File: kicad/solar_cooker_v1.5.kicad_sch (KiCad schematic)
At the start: 28 parts, among them J1 Pt100, J10 SSQ-108-01-G-S, J11 SSQ-108-01-G-S, J12 SSQ-108-01-G-S, J13 SSQ-118-01-G-D, J14 SSQ-108-01-G-S, J15 SSQ-108-01-G-S, J16 SSQ-110-01-G-S, J4 Pt100, J6 GPS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

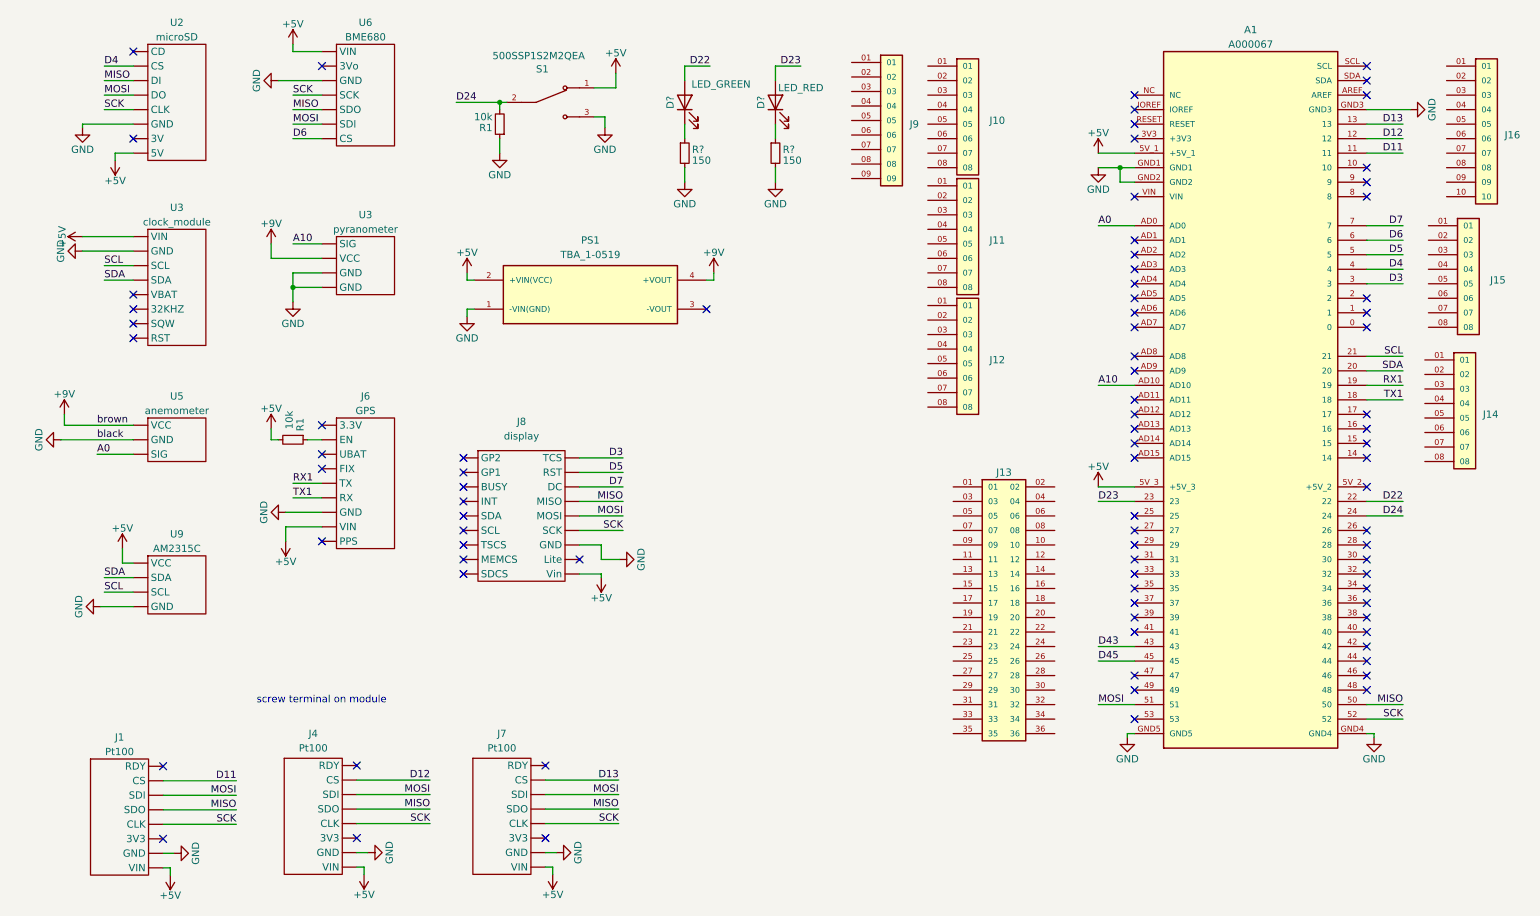
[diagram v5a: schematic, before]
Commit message: minor silkscreen fix
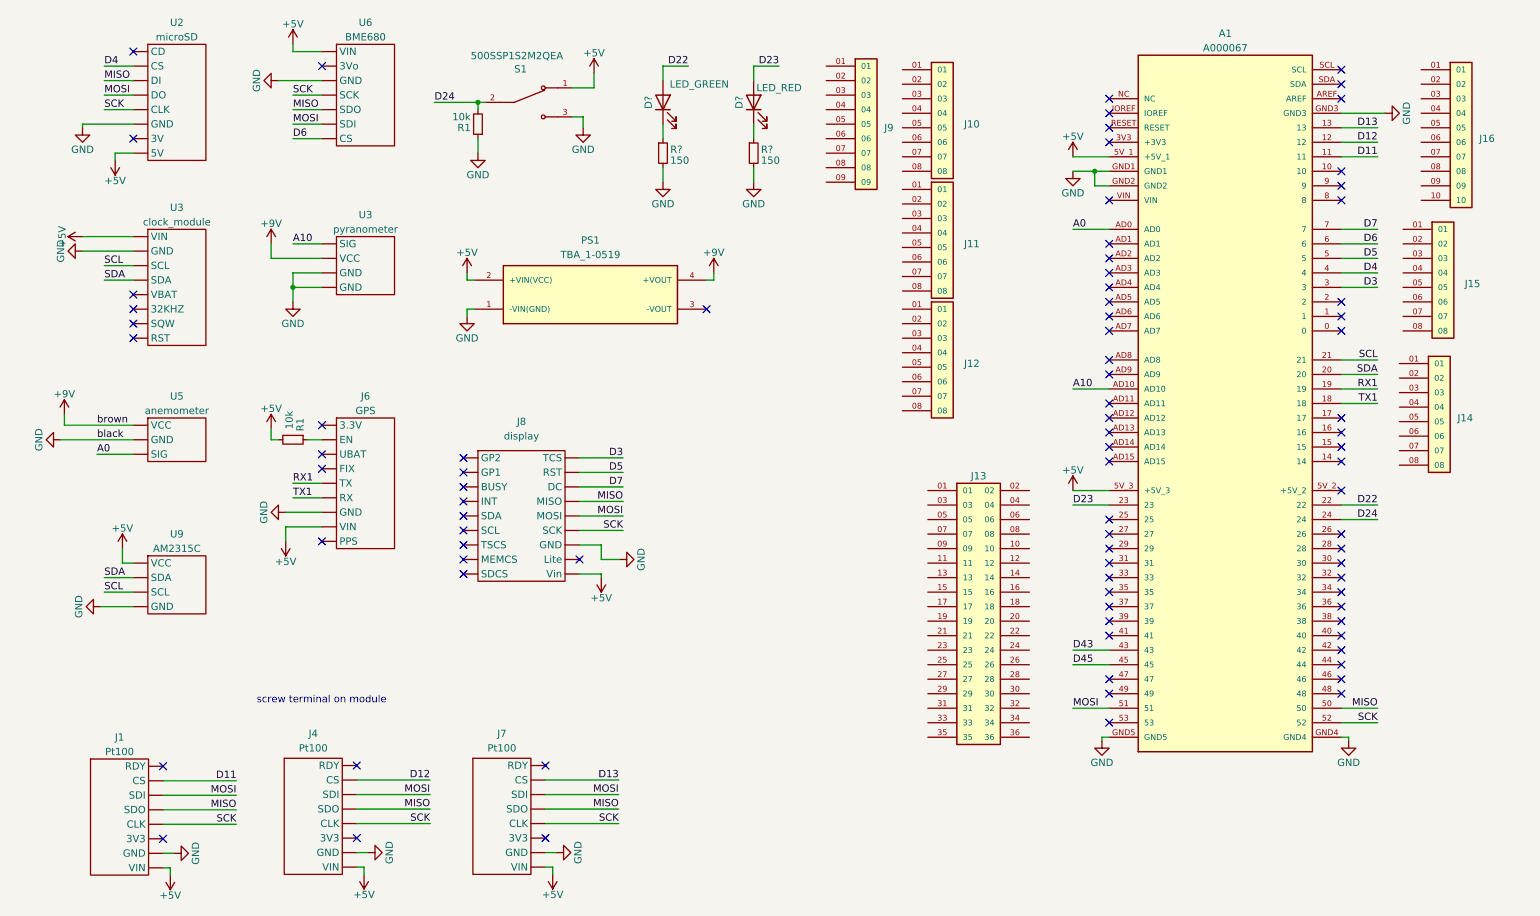
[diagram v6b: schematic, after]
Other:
- moved on the sheet: A1, D?, J10, J11, J12, J13, J14, J15, J16, J9, R1, R?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

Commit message: order v2
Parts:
- D? (x2): footprint (none) -> LED_SMD:LED_1206_3216Metric_Pad1.42x1.75mm_HandSolder
- J1, J4, J7: footprint custom_components:Pt100 -> custom_components:PT100
- J6: footprint (none) -> custom_components:GPS
- J8: footprint (none) -> custom_components:display
- PS1: footprint CONV_TBA_1-0519 -> TBA_1-0519:CONV_TBA_1-0519; MANUFACTURER Traco Power -> (none); MAXIMUM_PACKAGE_HEIGHT 10.15mm -> (none); PARTREV April 19, 2021 -> (none); STANDARD Manufacturer Recommendations -> (none)
- R1, R? (x2): footprint (none) -> Resistor_SMD:R_1206_3216Metric_Pad1.30x1.75mm_HandSolder
- U2: footprint (none) -> custom_components:microSD
- U3, U9: footprint (none) -> custom_components:screw_terminal_4pin
- U3: footprint (none) -> custom_components:clock_module
- U5: footprint (none) -> custom_components:screw_terminal_3pin
- U6: footprint (none) -> custom_components:BME680
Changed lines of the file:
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@@
     (stroke (width 0) (type default) (color 255 0 0 1))
+  )
+  (wire (pts (xy 208.915 57.785) (xy 215.265 57.785))
+    (stroke (width 0) (type default))
   )
   (wire (pts (xy 153.035 46.99) (xy 153.035 49.53))
@@
     (stroke (width 0) (type default))
   )
-  (wire (pts (xy 208.915 57.785) (xy 215.265 57.785))
-    (stroke (width 0) (type default))
-  )
   (wire (pts (xy 38.735 123.825) (xy 44.45 123.825))
     (stroke (width 0) (type default) (color 1 1 1 1))
@@
     (effects (font (size 1.27 1.27)) (justify left bottom))
   )
+  (label "A0" (at 208.915 57.785 0) (fields_autoplaced)
+    (effects (font (size 1.27 1.27)) (justify left bottom))
+  )
   (label "SCK" (at 62.484 161.925 180) (fields_autoplaced)
     (effects (font (size 1.27 1.27)) (justify right bottom))
@@
     (effects (font (size 1.27 1.27)) (justify left bottom))
   )
-  (label "A0" (at 208.915 57.785 0) (fields_autoplaced)
-    (effects (font (size 1.27 1.27)) (justify left bottom))
-  )
   (label "D12" (at 96.393 154.178 180) (fields_autoplaced)
     (effects (font (size 1.27 1.27)) (justify right bottom))
@@
       (effects (font (size 1.27 1.27)))
     )
-    (property "Footprint" "" (at 112.395 93.98 0)
+    (property "Footprint" "custom_components:display" (at 112.395 93.98 0)
       (effects (font (size 1.27 1.27)) hide)
     )
@@
       (effects (font (size 1.27 1.27)))
     )
-    (property "Footprint" "" (at 49.53 117.475 0)
+    (property "Footprint" "custom_components:screw_terminal_4pin" (at 49.53 117.475 0)
       (effects (font (size 1.27 1.27)) hide)
     )
@@
       (effects (font (size 1.27 1.27)) (justify left))
     )
-    (property "Footprint" "" (at 104.775 39.37 0)
+    (property "Footprint" "Resistor_SMD:R_1206_3216Metric_Pad1.30x1.75mm_HandSolder" (at 104.775 39.37 0)
       (effects (font (size 1.27 1.27)) hide)
     )
@@
       (effects (font (size 1.27 1.27)))
     )
-    (property "Footprint" "" (at 153.035 35.56 0)
+    (property "Footprint" "LED_SMD:LED_1206_3216Metric_Pad1.42x1.75mm_HandSolder" (at 153.035 35.56 0)
       (effects (font (size 1.27 1.27)) hide)
     )
@@
       (effects (font (size 1.27 1.27)) (justify left))
     )
-    (property "Footprint" "" (at 72.39 94.615 0)
+    (property "Footprint" "Resistor_SMD:R_1206_3216Metric_Pad1.30x1.75mm_HandSolder" (at 72.39 94.615 0)
       (effects (font (size 1.27 1.27)) hide)
     )
@@
       (effects (font (size 1.27 1.27)))
     )
-    (property "Footprint" "" (at 52.07 27.94 0)
+    (property "Footprint" "custom_components:microSD" (at 52.07 27.94 0)
       (effects (font (size 1.27 1.27)) hide)
     )
@@
       (effects (font (size 1.27 1.27)) (justify left))
     )
-    (property "Footprint" "" (at 153.035 44.45 0)
+    (property "Footprint" "Resistor_SMD:R_1206_3216Metric_Pad1.30x1.75mm_HandSolder" (at 153.035 44.45 0)
       (effects (font (size 1.27 1.27)) hide)
     )
@@
       (effects (font (size 1.27 1.27)))
     )
-    (property "Footprint" "custom_components:Pt100" (at 73.406 149.098 0)
+    (property "Footprint" "custom_components:PT100" (at 73.406 149.098 0)
       (effects (font (size 1.27 1.27)) hide)
     )
@@
       (effects (font (size 1.27 1.27)))
     )
-    (property "Footprint" "" (at 137.16 35.56 0)
+    (property "Footprint" "LED_SMD:LED_1206_3216Metric_Pad1.42x1.75mm_HandSolder" (at 137.16 35.56 0)
       (effects (font (size 1.27 1.27)) hide)
     )
@@
       (effects (font (size 1.27 1.27)))
     )
-    (property "Footprint" "" (at 85.09 60.325 0)
+    (property "Footprint" "custom_components:screw_terminal_4pin" (at 85.09 60.325 0)
       (effects (font (size 1.27 1.27)) hide)
     )
@@
       (effects (font (size 1.27 1.27)))
     )
-    (property "Footprint" "custom_components:Pt100" (at 39.497 149.225 0)
+    (property "Footprint" "custom_components:PT100" (at 39.497 149.225 0)
       (effects (font (size 1.27 1.27)) hide)
     )
@@
       (effects (font (size 1.27 1.27)))
     )
-    (property "Footprint" "custom_components:Pt100" (at 106.426 149.098 0)
+    (property "Footprint" "custom_components:PT100" (at 106.426 149.098 0)
       (effects (font (size 1.27 1.27)) hide)
     )
@@
       (effects (font (size 1.27 1.27)) (justify left))
     )
-    (property "Footprint" "" (at 137.16 44.45 0)
+    (property "Footprint" "Resistor_SMD:R_1206_3216Metric_Pad1.30x1.75mm_HandSolder" (at 137.16 44.45 0)
       (effects (font (size 1.27 1.27)) hide)
     )
@@
       (effects (font (size 1.27 1.27)))
     )
-    (property "Footprint" "" (at 53.34 98.425 0)
+    (property "Footprint" "custom_components:screw_terminal_3pin" (at 53.34 98.425 0)
       (effects (font (size 1.27 1.27)) hide)
     )
@@
   (symbol (lib_id "A000067:A000067") (at 235.585 88.265 0) (unit 1)
     (in_bom no) (on_board yes) (dnp no) (fields_autoplaced)
-    (property "Reference" "A1" (at 235.585 23.495 0)
-      (effects (font (size 1.27 1.27)))
-    )
-    (property "Value" "A000067" (at 235.585 26.035 0)
+    (property "Reference" "A1" (at 235.585 22.86 0)
+      (effects (font (size 1.27 1.27)))
+    )
+    (property "Value" "A000067" (at 235.585 25.4 0)
       (effects (font (size 1.27 1.27)))
     )
@@
     (pin "8")
     (pin "9")
-    (pin "AD0")
     (pin "AD1")
     (pin "AD10")
@@
     (pin "SDA")
     (pin "VIN")
+    (pin "AD0")
     (instances
       (project "solar_cooker_v1.5"
@@
       (effects (font (size 1.27 1.27)))
     )
-    (property "Footprint" "" (at 87.63 34.29 0)
+    (property "Footprint" "custom_components:BME680" (at 87.63 34.29 0)
       (effects (font (size 1.27 1.27)) hide)
     )
@@
       (effects (font (size 1.27 1.27)))
     )
-    (property "Footprint" "" (at 85.09 90.805 0)
+    (property "Footprint" "custom_components:GPS" (at 85.09 90.805 0)
       (effects (font (size 1.27 1.27)) hide)
     )
@@
       (effects (font (size 1.27 1.27)))
     )
-    (property "Footprint" "" (at 52.07 67.945 0)
+    (property "Footprint" "custom_components:clock_module" (at 52.07 67.945 0)
       (effects (font (size 1.27 1.27)) hide)
     )
@@
       (effects (font (size 1.27 1.27)))
     )
-    (property "Footprint" "CONV_TBA_1-0519" (at 124.46 69.215 0)
+    (property "Footprint" "TBA_1-0519:CONV_TBA_1-0519" (at 124.46 69.215 0)
       (effects (font (size 1.27 1.27)) (justify bottom) hide)
     )
@@
       (effects (font (size 1.27 1.27)) hide)
     )
-    (property "PARTREV" "April 19, 2021" (at 124.46 69.215 0)
-      (effects (font (size 1.27 1.27)) (justify bottom) hide)
-    )
-    (property "STANDARD" "Manufacturer Recommendations" (at 124.46 69.215 0)
-      (effects (font (size 1.27 1.27)) (justify bottom) hide)
-    )
-    (property "MAXIMUM_PACKAGE_HEIGHT" "10.15mm" (at 124.46 69.215 0)
-      (effects (font (size 1.27 1.27)) (justify bottom) hide)
-    )
-    (property "MANUFACTURER" "Traco Power" (at 124.46 69.215 0)
-      (effects (font (size 1.27 1.27)) (justify bottom) hide)
-    )
     (property "Description" "DC DC CONVERTER 9V 990MW" (at 124.46 69.215 0)

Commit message: BOM generation update
now uses KiBoM
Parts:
- J1, J4, J7: footprint custom_components:PT100 -> custom_components:Pt100
- S1: footprint SW_500SSP1S2M2QEA -> 500SSP1S2M2QEA:SW_500SSP1S2M2QEA; MANUFACTURER E-switch -> (none); MAXIMUM_PACKAGE_HEIGHT 13.59mm -> (none); PARTREV C -> (none); STANDARD Manufacturer Recommendations -> (none)
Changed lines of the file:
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@@
       (effects (font (size 1.27 1.27)))
     )
-    (property "Footprint" "custom_components:PT100" (at 73.406 149.098 0)
+    (property "Footprint" "custom_components:Pt100" (at 73.406 149.098 0)
       (effects (font (size 1.27 1.27)) hide)
     )
@@
       (effects (font (size 1.27 1.27)))
     )
-    (property "Footprint" "custom_components:PT100" (at 39.497 149.225 0)
+    (property "Footprint" "custom_components:Pt100" (at 39.497 149.225 0)
       (effects (font (size 1.27 1.27)) hide)
     )
@@
       (effects (font (size 1.27 1.27)))
     )
-    (property "Footprint" "custom_components:PT100" (at 106.426 149.098 0)
+    (property "Footprint" "custom_components:Pt100" (at 106.426 149.098 0)
       (effects (font (size 1.27 1.27)) hide)
     )
@@
       (effects (font (size 1.27 1.27)) (justify left top))
     )
-    (property "Footprint" "SW_500SSP1S2M2QEA" (at 113.665 35.56 0)
+    (property "Footprint" "500SSP1S2M2QEA:SW_500SSP1S2M2QEA" (at 113.665 35.56 0)
       (effects (font (size 1.27 1.27)) (justify bottom) hide)
     )
@@
       (effects (font (size 1.27 1.27)) hide)
     )
-    (property "PARTREV" "C" (at 113.665 35.56 0)
-      (effects (font (size 1.27 1.27)) (justify bottom) hide)
-    )
-    (property "STANDARD" "Manufacturer Recommendations" (at 113.665 35.56 0)
-      (effects (font (size 1.27 1.27)) (justify bottom) hide)
-    )
-    (property "MAXIMUM_PACKAGE_HEIGHT" "13.59mm" (at 113.665 35.56 0)
-      (effects (font (size 1.27 1.27)) (justify bottom) hide)
-    )
-    (property "MANUFACTURER" "E-switch" (at 113.665 35.56 0)
-      (effects (font (size 1.27 1.27)) (justify bottom) hide)
-    )
     (property "Description" "Slide Switch" (at 113.665 35.56 0)
